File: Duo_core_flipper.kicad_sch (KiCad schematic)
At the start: 24 parts

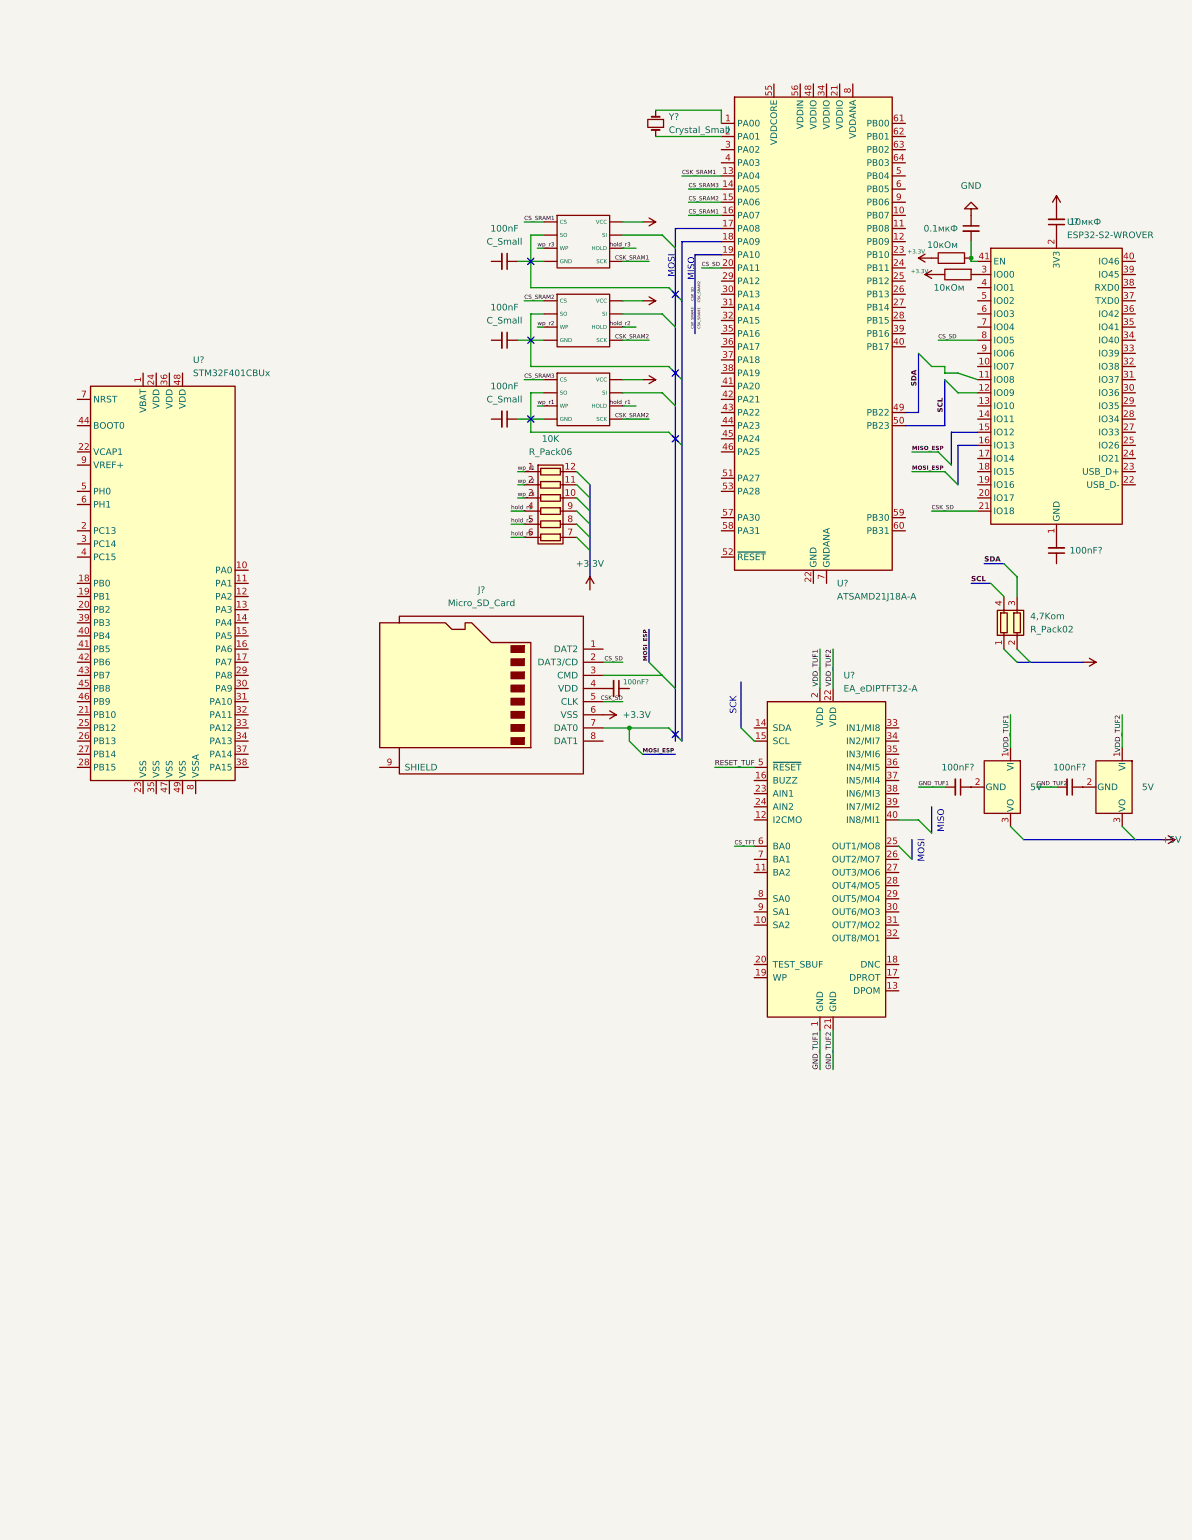
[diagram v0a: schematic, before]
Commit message: add atmega128 to SAMD21
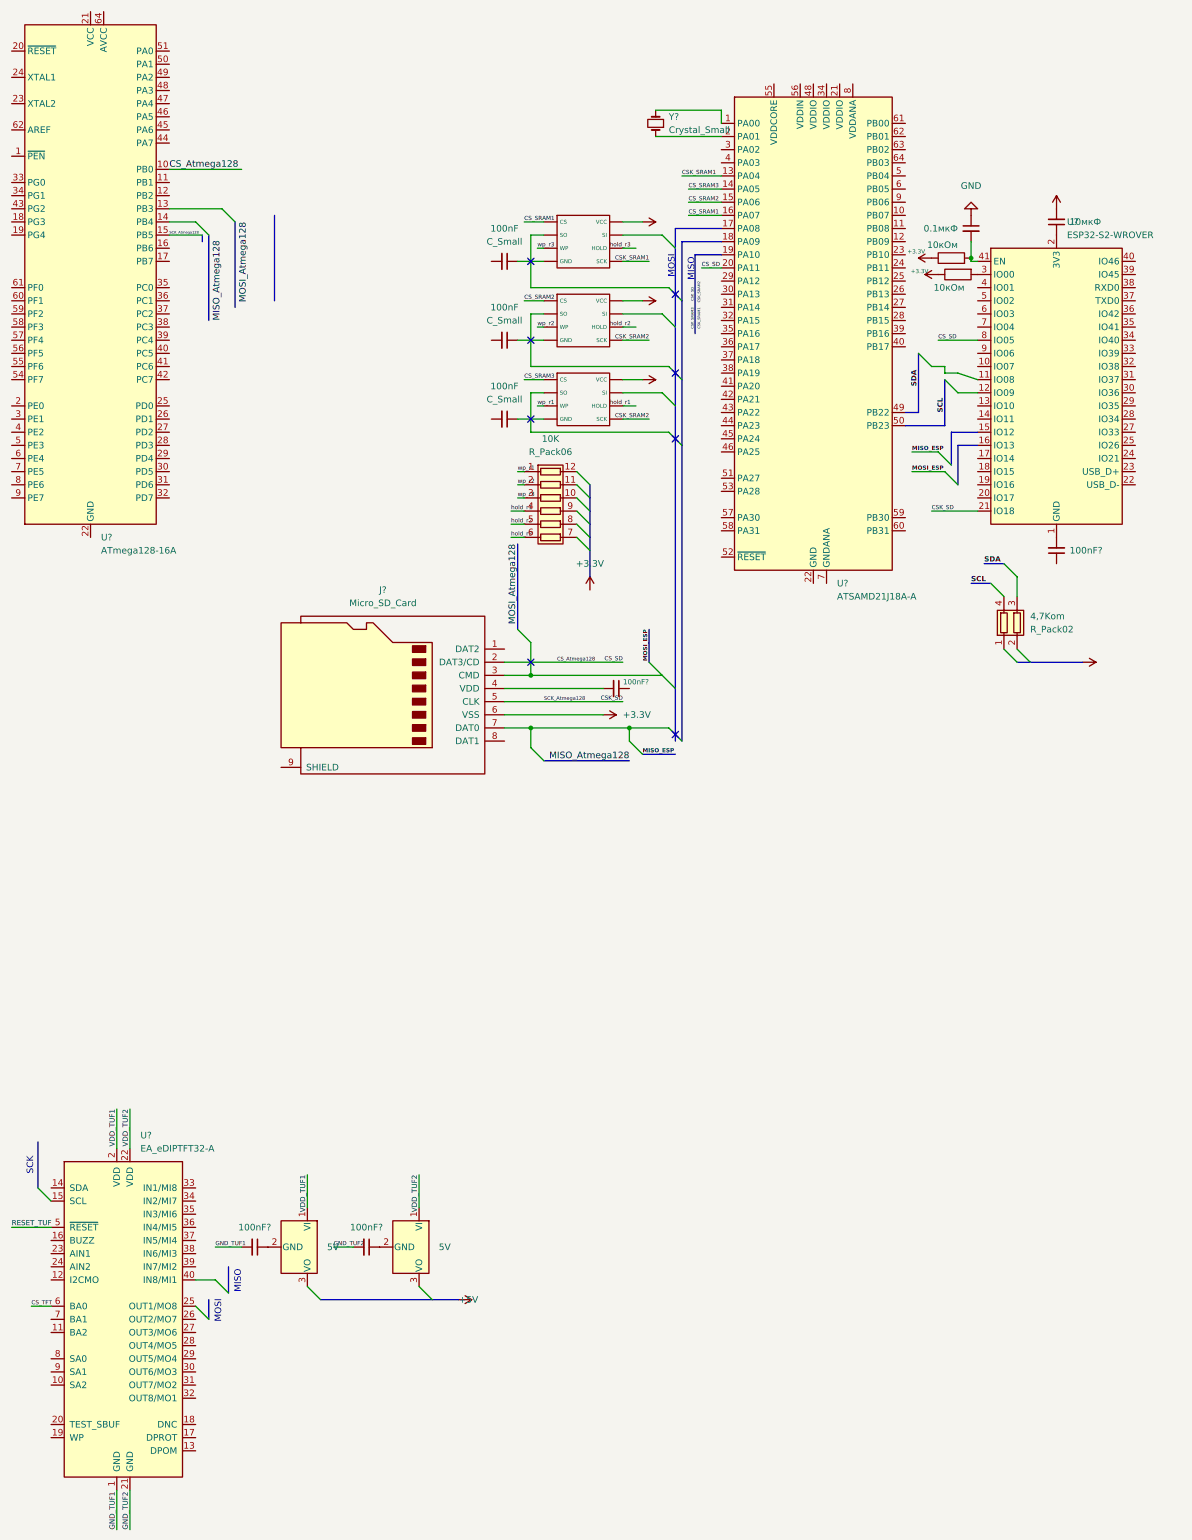
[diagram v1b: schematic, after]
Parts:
- removed U?: STM32F401CBUx, Package_DFN_QFN:QFN-48-1EP_7x7mm_P0.5mm_EP5.6x5.6mm, symbol MCU_ST_STM32F4:STM32F401CBUx
- added U?: ATmega128-16A, Package_QFP:TQFP-64_14x14mm_P0.8mm, symbol MCU_Microchip_ATmega:ATmega128-16A
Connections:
- net CSK_SD: now also U?.15 (PB5)
- net CS_SD renamed CS_Atmega128
- net CS_Atmega128: now also U?.10 (PB0)
- new net: U?.21 (VCC), U?.52 (VCC)
- new net: U?.22 (GND), U?.53 (GND), U?.63 (GND)
- no-connect marks 7 -> 8
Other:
- moved on the sheet: 100nF?, 5V, J?, U?
